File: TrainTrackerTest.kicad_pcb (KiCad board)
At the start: 2 copper layers, 51.2 x 53.8 mm, 18 parts, among them J1 PJ-002B, J2 Conn_01x15_Socket, J3 Conn_01x15_Socket, U1 TLC5955DCAR, U2 TLC5955DCAR

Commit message: Finalize test board pcb layout
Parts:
- J1: footprint TrainTrackerTest_mod:PJ-002B_CUI -> TrainTrackerTest_mod:CUI_PJ-002B
- moved J1 2.16 mm to (105.4, 98.7), turned to 0 degrees
- moved C1 1.84 mm to (100.8, 95.9)
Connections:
- U1 pad V: (no net) -> GND
- U2 pad V: (no net) -> GND
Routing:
- net GND: track 53.6 -> 62.8 mm, vias 7 -> 8
- net /5V: track 93.0 -> 99.7 mm
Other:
- board text added: "Train Tracker Test Board 1 March 2025"

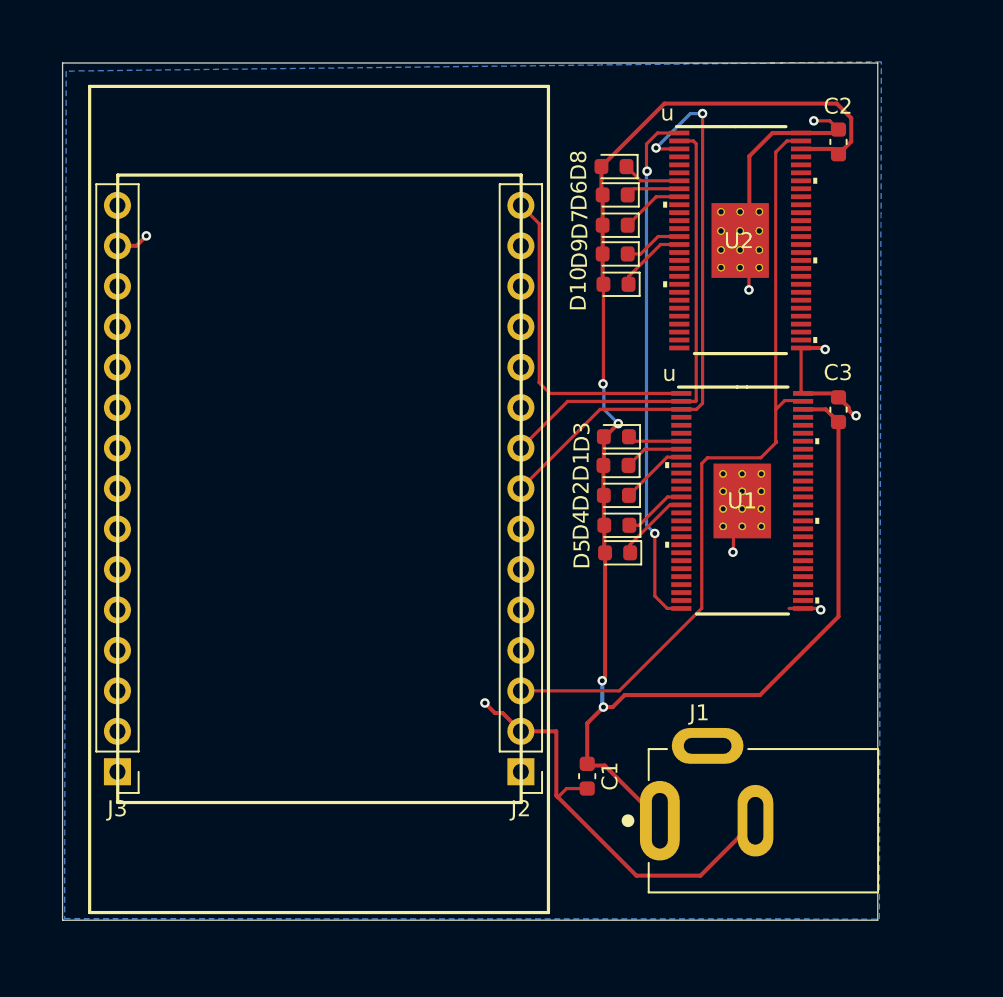
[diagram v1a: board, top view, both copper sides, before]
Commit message: Change 1000uF footprint
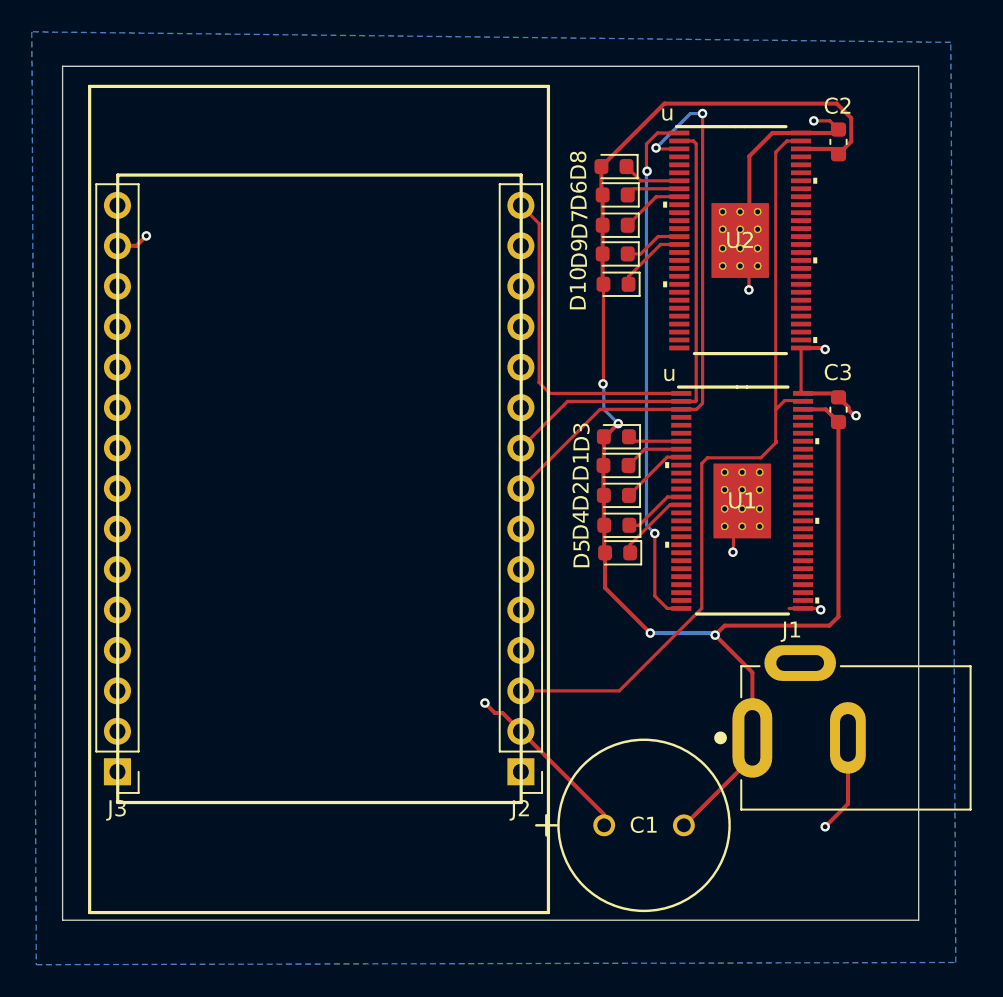
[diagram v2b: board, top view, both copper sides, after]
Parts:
- C1: value 1000uF -> 10ZLH1000MEFC10X12.5; footprint Capacitor_SMD:C_0603_1608Metric -> TrainTrackerTest_mod:CAP_10X12.5_RUB
- moved J1 7.80 mm to (111.2, 93.5)
- moved C1 3.26 mm to (101.9, 99.0), turned to 0 degrees
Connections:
- C1 pad 1: /5V -> GND
- C1 pad 2: GND -> /5V
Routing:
- net GND: track 62.8 -> 52.8 mm, vias 8 -> 9
- net /5V: track 99.7 -> 96.1 mm
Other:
- board size 51.2 x 53.8 mm -> 53.8 x 53.6 mm
